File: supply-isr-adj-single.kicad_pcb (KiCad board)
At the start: 2 copper layers, 35.1 x 39.4 mm, 26 parts, among them P1 CONN_02X02, P2 CONN_01X03, P3 CONN_02X04, P4 CONN_02X08, P5 CONN_01X01, P6 CONN_01X01, U1 TPS54232DR

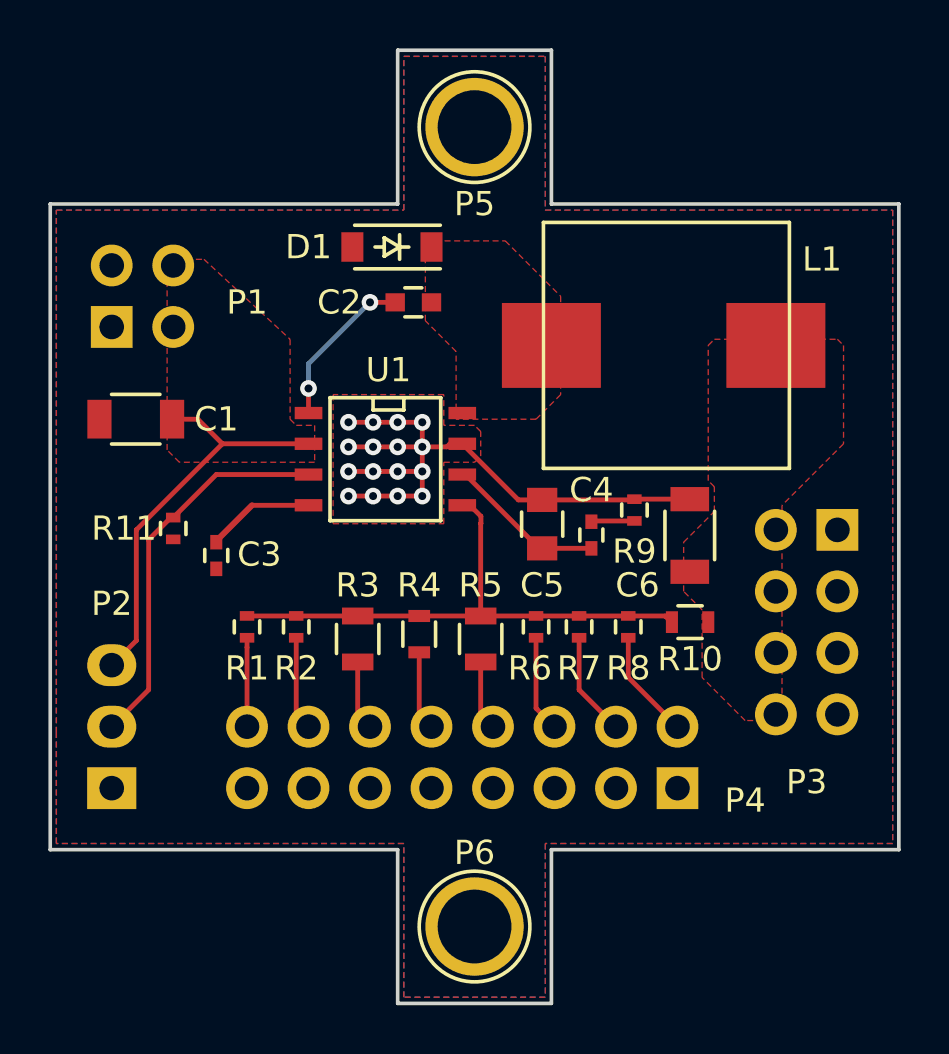
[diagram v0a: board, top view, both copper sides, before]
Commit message: Limit EN pin voltage Add LED port
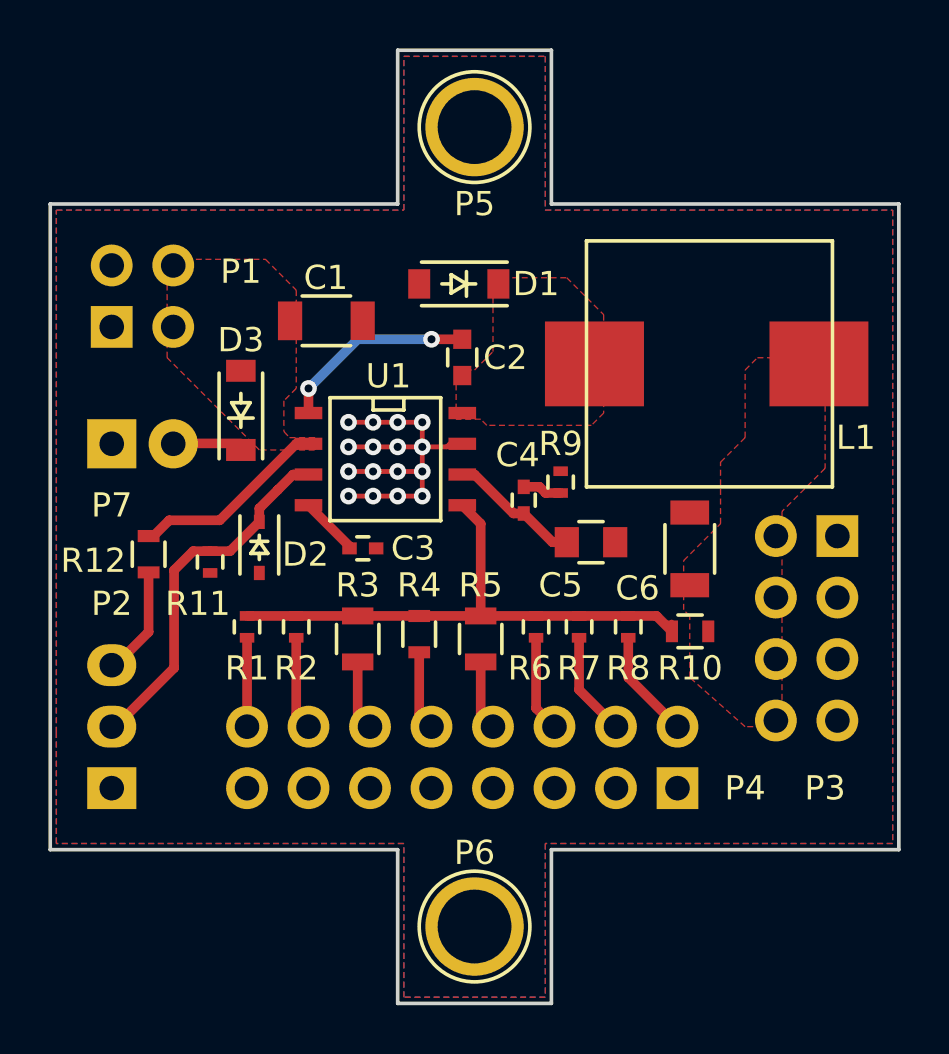
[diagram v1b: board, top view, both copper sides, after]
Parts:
- added D2: DZ2J047M0L, Diodes_SMD:SOD-323, F.Cu at (79.0, 47.2)
- added D3: NSI45015WT1G, Diodes_SMD:SOD-123, F.Cu at (78.2, 41.5)
- added P7: CONN_01X02, Pin_Headers:Pin_Header_Straight_1x02, B.Cu at (72.9, 42.9)
- added R12: RC0603FR-0717K8L, Resistors_SMD:R_0603, F.Cu at (74.4, 47.5)
- moved C1 8.86 mm to (81.8, 37.8), turned to 0 degrees
- moved C3 6.06 mm to (83.3, 47.2), turned to 0 degrees
- moved R9 3.26 mm to (91.4, 44.5)
- moved D1 3.15 mm to (87.2, 36.3)
- moved C4 3.14 mm to (89.9, 45.3)
- moved C2 3.04 mm to (87.4, 39.4), turned to 90 degrees
- moved C5 2.15 mm to (92.7, 47.0), turned to 0 degrees
- moved R11 2.06 mm to (77.0, 47.8)
- moved L1 1.93 mm to (97.6, 39.6)
- moved C6 0.56 mm to (96.8, 47.3)
- moved R10 0.38 mm to (96.8, 50.7)
- moved P3 0.25 mm to (102.9, 46.7)
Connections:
- P2 pad 3: /Vin -> Net-(P2-Pad3)
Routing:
- net GND: track 27.5 -> 17.1 mm
- net /Vin: track 17.1 -> 8.18 mm
- net Net-(P2-Pad3): track 0.00 -> 4.55 mm
- net Net-(D3-Pad1): track 0.00 -> 2.80 mm
- net Net-(C3-Pad1): track 4.47 -> 2.48 mm
- net Net-(C2-Pad2): track 6.66 -> 8.21 mm
- net Net-(C4-Pad1): track 6.98 -> 5.92 mm
- net Net-(D2-Pad1): track 16.1 -> 15.1 mm
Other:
- net class Default: clearance 0.2 -> 0.4; trace_width 0.2 -> 0.4
- rule trace_clearance: 0.2 -> 0.4
- board text added: "LED"
